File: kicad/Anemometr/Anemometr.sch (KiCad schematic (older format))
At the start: 158 parts, among them J1 Conn_01x01_Female, J10 +Z3, J11 -Z3, J12 +Z4, J13 -Z4, J14 SWD, J15 SWC, J16 Z4, J17 Z4, J18 1, J19 2, J2 Conn_01x01_Female, J20 3, J21 4, J22 5, J23 6, J24 7, J25 8, J26 Z4, J27 Z4, J28 Z4, J29 Z4, J3 RST, J30 Z4, J31 Z4, J32 Z4, J33 Z4, J34 Z4, J35 Z4, J4 TxD, J5 RxD, J6 +Z1, J7 -Z1, J8 +Z2, J9 -Z2, U1 TS5A3166DBVR, U10 MCP1700-3002E, U2 LMV7239, U3 TS5A3166DBVR, U4 TS5A3166DBVR, U5 STM32F103C8Tx, U6 TS5A3166DBVR, U7 LM2734Y, U8 MCP1700-5002E, U9 MCP1700-3002E, Y1 8MHz, Y2 25MHz

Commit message: изменено:      Documents/circuit.png 	изменено:      kicad/Anemometr/Anemometr.pdf 	изменено:      kicad/Anemometr/Anemometr.sch 	изменено:      kicad/Anemometr/Anemometr.sch-bak
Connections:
- net at C22.2, D2.2 (A), U7.4 (EN)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: now also L5.1
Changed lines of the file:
@@
 Wire Wire Line
 	9700 1800 9700 2000
+Wire Wire Line
+	11500 4900 8150 4900
+Wire Wire Line
+	8150 4900 8150 3500
+Wire Wire Line
+	8150 3500 8550 3500
+Connection ~ 8550 3500
 $EndSCHEMATC

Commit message: изменено:      Documents/circuit.png 	изменено:      kicad/Anemometr/Anemometr.pdf 	изменено:      kicad/Anemometr/Anemometr.sch 	изменено:      kicad/Anemometr/Anemometr.sch-bak
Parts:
- J18: value 1 -> 1 TxD+
- J19: value 2 -> 2 TxD-
- J20: value 3 -> 3 RxD+
- J23: value 6 -> 6 RxD-
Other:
- moved on the sheet: C35, C38, C39, C40, C41, C42, C43, C44, C45, C46, C47, C48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

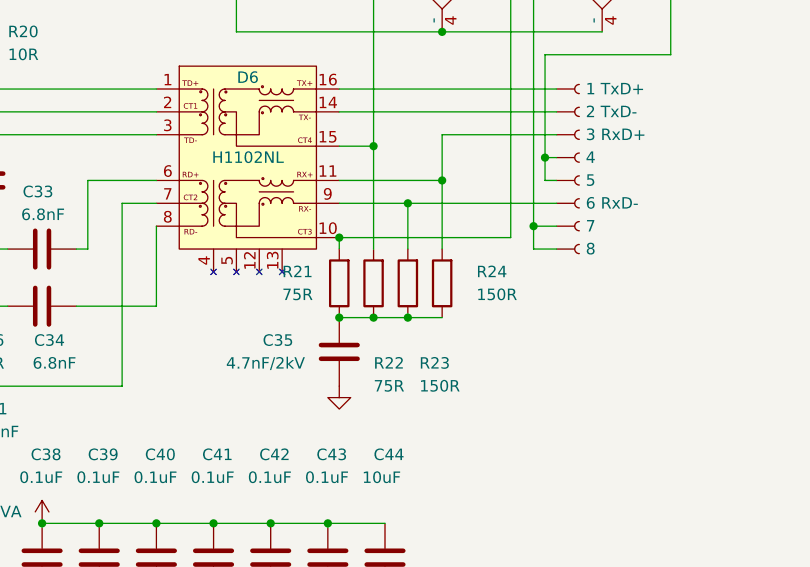
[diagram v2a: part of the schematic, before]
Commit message: изменено:      kicad/Anemometr/Anemometr-cache.lib 	изменено:      kicad/Anemometr/Anemometr-rescue.lib 	изменено:      kicad/Anemometr/Anemometr.kicad_pcb 	изменено:      kicad/Anemometr/Anemometr.kicad_pcb-bak 	изменено:      kicad/Anemometr/Anemometr.sch 	изменено:      kicad/Anemometr/Anemometr.sch-bak 	изменено:      kicad/Anemometr/fp-info-cache
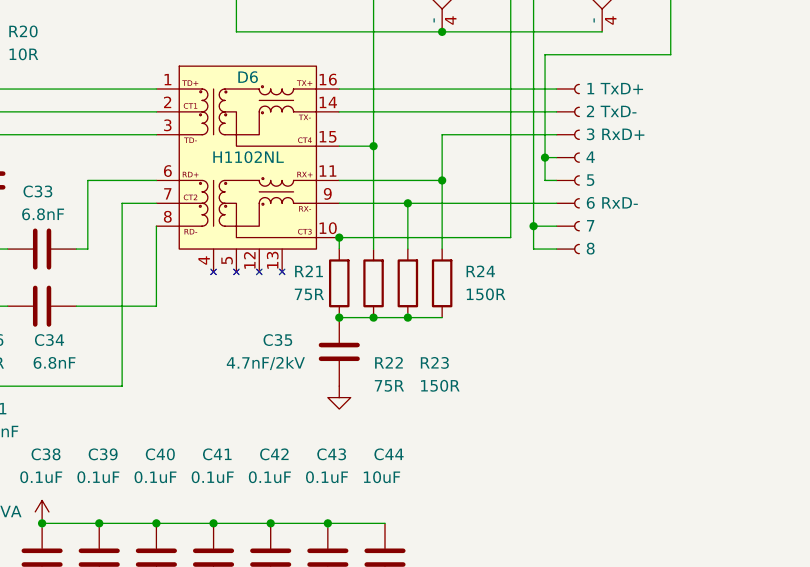
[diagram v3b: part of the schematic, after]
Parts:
- C49: footprint Capacitor_SMD:C_0805_2012Metric -> Capacitor_SMD:C_1210_3225Metric
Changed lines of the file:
@@
 U 1 1 61FFF702
 P 9950 8100
-F 0 "R21" H 10200 8050 50  0000 R CNN
-F 1 "75R" H 10200 8150 50  0000 R CNN
+F 0 "R21" H 10150 8050 50  0000 R CNN
+F 1 "75R" H 10150 8150 50  0000 R CNN
 F 2 "Resistor_SMD:R_0402_1005Metric" V 9880 8100 50  0001 C CNN
 F 3 "~" H 9950 8100 50  0001 C CNN
@@
 U 1 1 6211700D
 P 10400 8100
-F 0 "R24" H 10250 8050 50  0000 R CNN
-F 1 "150R" H 10250 8150 50  0000 R CNN
+F 0 "R24" H 10300 8050 50  0000 R CNN
+F 1 "150R" H 10300 8150 50  0000 R CNN
 F 2 "Resistor_SMD:R_0402_1005Metric" V 10330 8100 50  0001 C CNN
 F 3 "~" H 10400 8100 50  0001 C CNN
@@
 F 0 "C49" H 11400 5200 50  0000 L CNN
 F 1 "20uF" H 11400 5100 50  0000 L CNN
-F 2 "Capacitor_SMD:C_0805_2012Metric" H 11688 5250 50  0001 C CNN
+F 2 "Capacitor_SMD:C_1210_3225Metric" H 11688 5250 50  0001 C CNN
 F 3 "~" H 11650 5400 50  0001 C CNN
 	1    11650 5400

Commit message: изменено:      kicad/Anemometr/Anemometr.kicad_pcb 	изменено:      kicad/Anemometr/Anemometr.kicad_pcb-bak 	изменено:      kicad/Anemometr/Anemometr.sch 	изменено:      kicad/Anemometr/Anemometr.sch-bak 	изменено:      kicad/Anemometr/fp-info-cache
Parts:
- C1, C2, C3, C4, C5, C6, C7, C8: footprint Capacitor_SMD:C_0805_2012Metric -> Capacitor_SMD:C_0603_1608Metric
- R10, R11, R2, R3, R36, R37, R38, R39, R4, R5, R6, R7, R8, R9: footprint Resistor_SMD:R_0805_2012Metric -> Resistor_SMD:R_0603_1608Metric
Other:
- moved on the sheet: C47, R32
